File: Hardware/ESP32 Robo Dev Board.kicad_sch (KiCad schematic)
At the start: 49 parts, among them J2 Conn_01x02_Pin, Q1 DMP2045U, SW1 SW_Push_Dual_x2, SW2 SW_Push, U1 ESP32-S3-WROOM-1, U2 TCA9548ARGER, U8 MCP73831-2-OT, U9 AP2112K-3.3

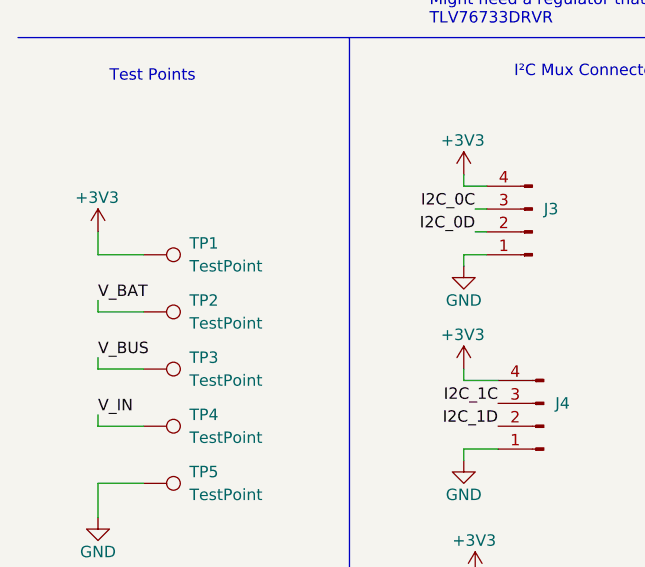
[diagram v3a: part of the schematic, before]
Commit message: Fix DRC Errors
Silkscreen overlapping and some trace width modification.
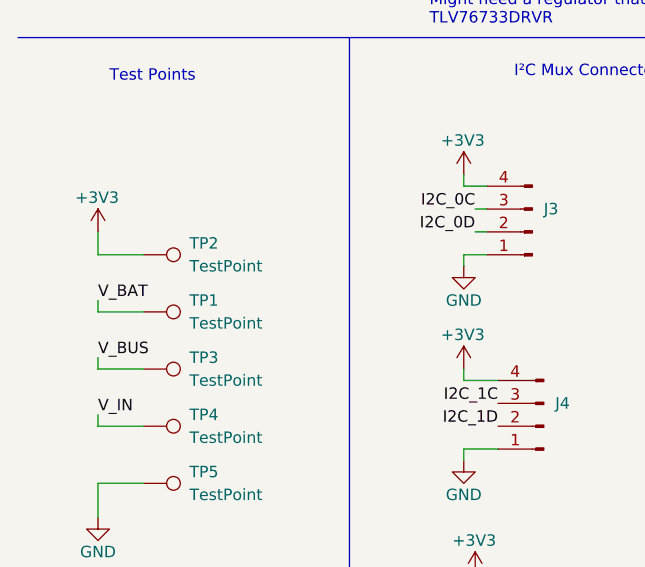
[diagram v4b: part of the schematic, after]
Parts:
- renumbered TP2 to TP1, TP1 to TP2
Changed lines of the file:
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@@
 		(dnp no)
 		(fields_autoplaced yes)
-		(property "Reference" "TP2"
-			(at 31.75 106.68 90)
+		(property "Reference" "TP1"
+			(at 31.75 106.6799 90)
 			(effects
 				(font
@@
 		)
 		(property "Value" "TestPoint"
-			(at 31.75 109.22 90)
+			(at 31.75 109.2199 90)
 			(effects
 				(font
@@
 			(project "ESP32 Robo Dev Board"
 				(path "/e63e39d7-6ac0-4ffd-8aa3-1841a4541b55"
-					(reference "TP2")
+					(reference "TP1")
 					(unit 1)
 				)
@@
 		(dnp no)
 		(fields_autoplaced yes)
-		(property "Reference" "TP1"
-			(at 31.75 100.33 90)
+		(property "Reference" "TP2"
+			(at 31.75 100.3299 90)
 			(effects
 				(font
@@
 		)
 		(property "Value" "TestPoint"
-			(at 31.75 102.87 90)
+			(at 31.75 102.8699 90)
 			(effects
 				(font
@@
 			(project "ESP32 Robo Dev Board"
 				(path "/e63e39d7-6ac0-4ffd-8aa3-1841a4541b55"
-					(reference "TP1")
-					(unit 1)
-				)
+					(reference "TP2")
+					(unit 1)
+				)

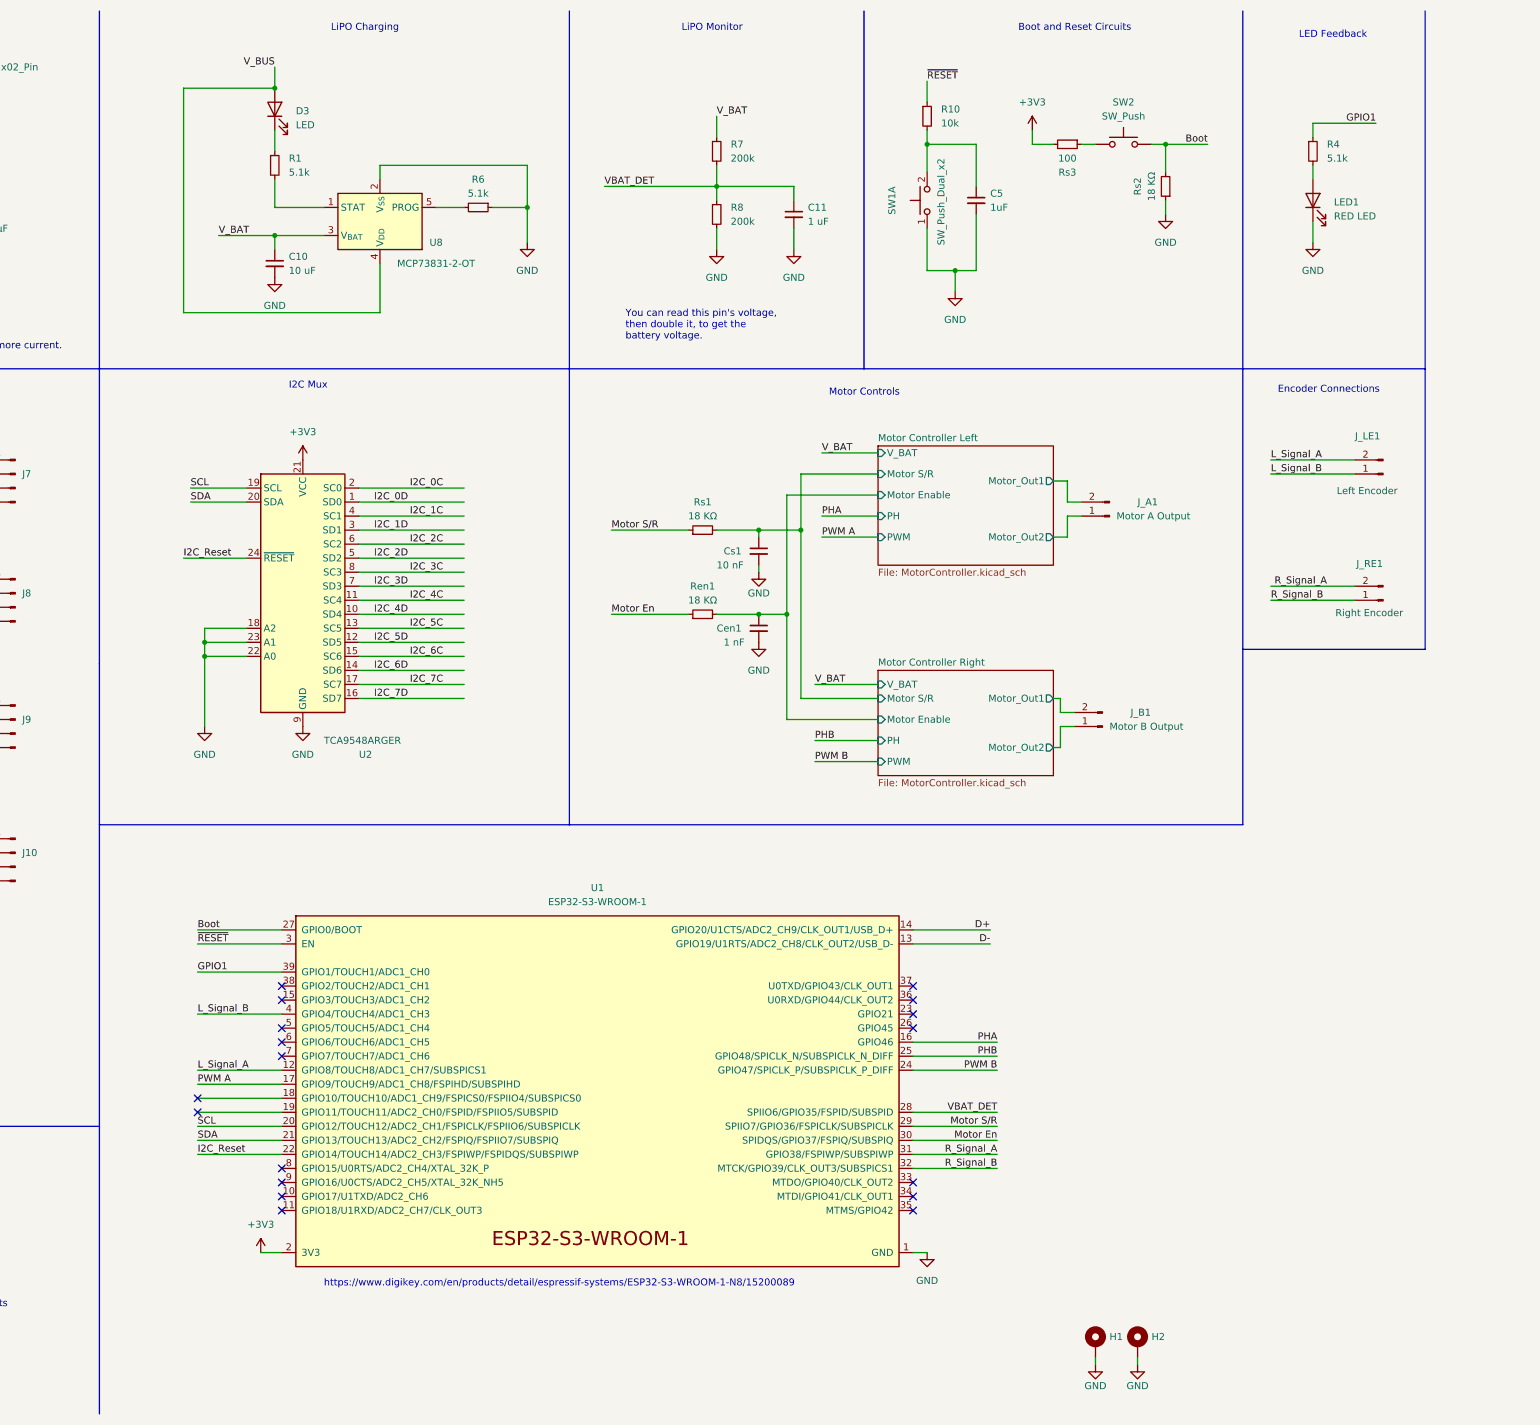
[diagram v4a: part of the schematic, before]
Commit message: Standardize I²C Bus and Route USB-C
Taking the opportunity to reroute and place STEMMA QT (JST-SH) Connectors to standardize the use of the I²C Multiplexer. Also took the chance to clean up the USB-C power supply and data line routing.
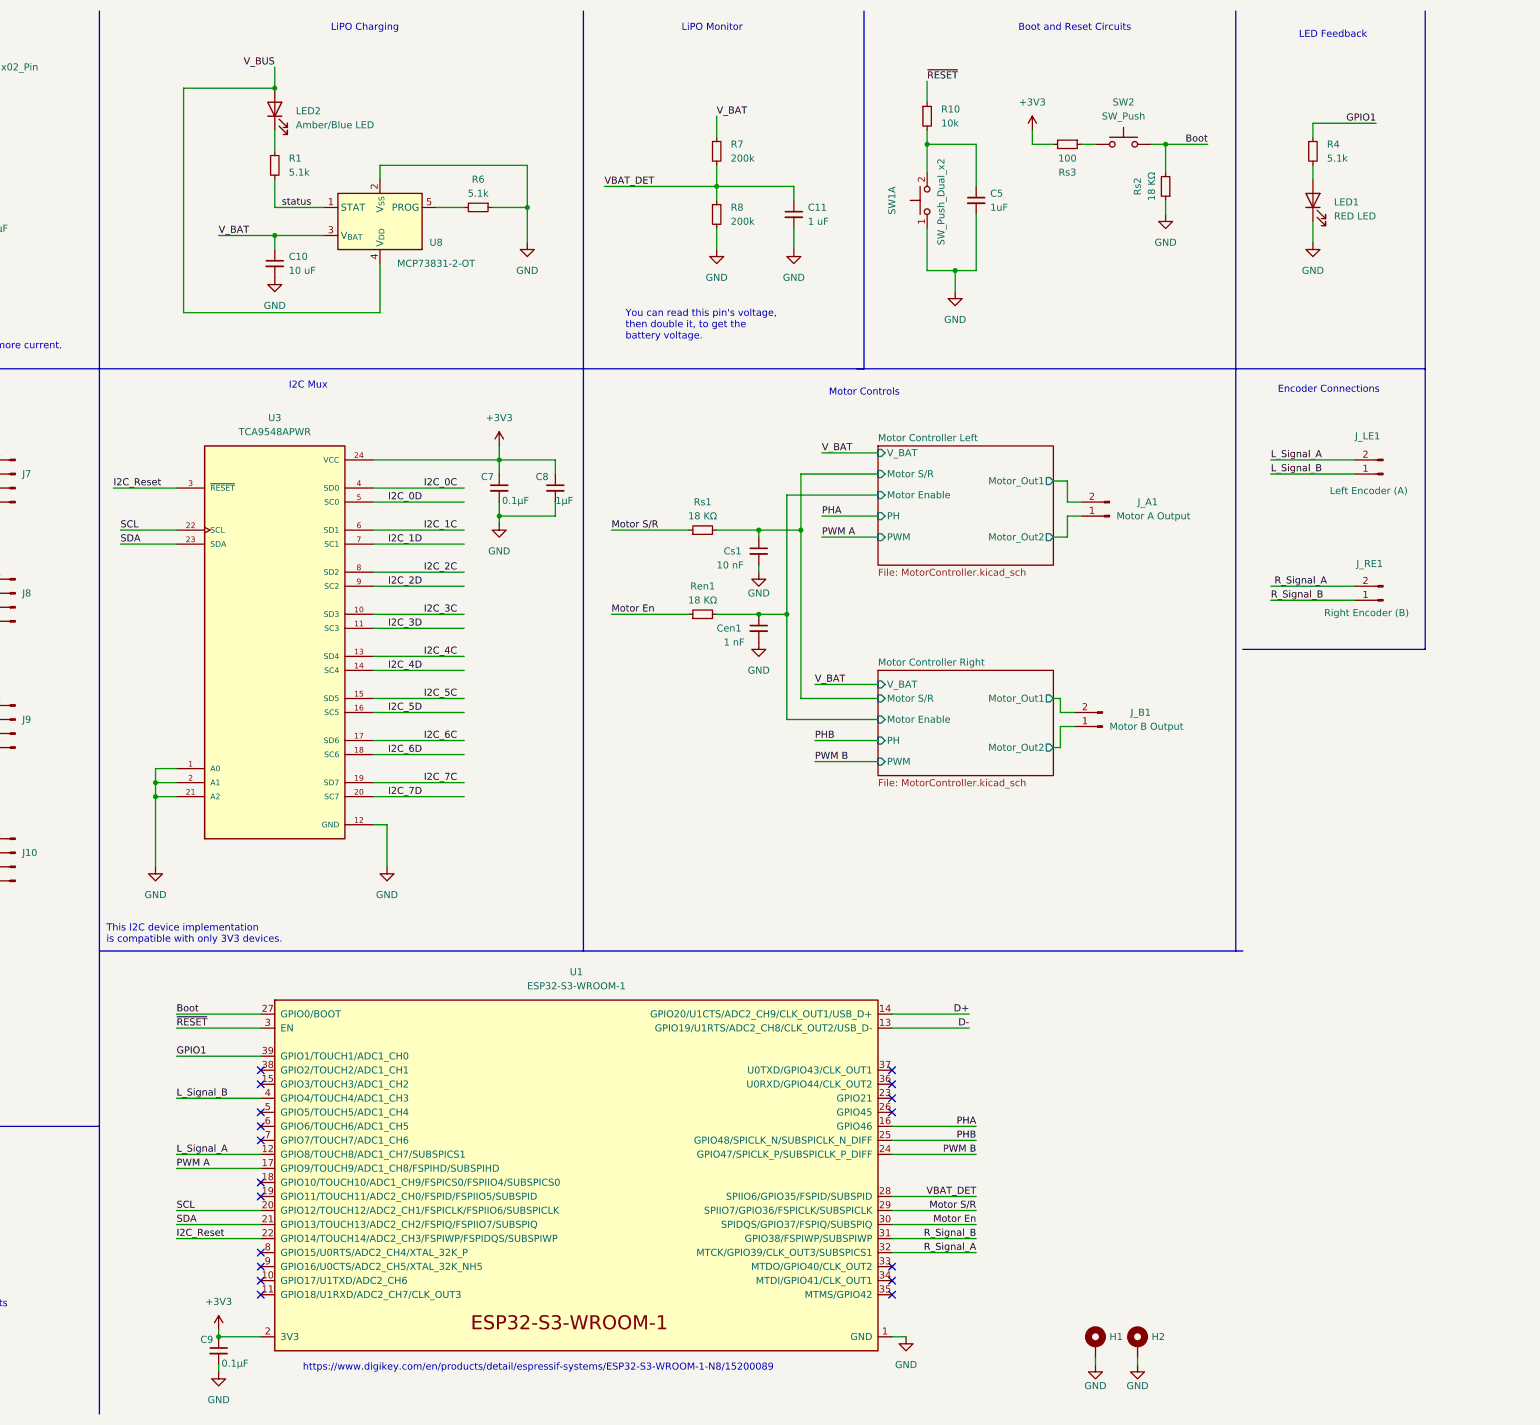
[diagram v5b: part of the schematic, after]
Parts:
- removed U2: TCA9548ARGER, Package_SO:TSSOP-24_4.4x7.8mm_P0.65mm, symbol Interface_Expansion:TCA9548ARGER
- added C7, C9: 0.1μF, Capacitor_SMD:C_0603_1608Metric, symbol Device:C_Small
- added C8: 1μF, Capacitor_SMD:C_0603_1608Metric, symbol Device:C_Small
- added U3: TCA9548APWR, TCA9548APWR:SOP65P640X120-24N, symbol TCA9548APWR:TCA9548APWR
- C1: footprint Capacitor_SMD:C_1206_3216Metric_Pad1.33x1.80mm_HandSolder -> Capacitor_SMD:C_0805_2012Metric
- J10, J3, J4, J5, J6, J7, J8, J9: footprint Connector_PinHeader_1.00mm:PinHeader_1x04_P1.00mm_Vertical -> Connector_JST:JST_SH_SM04B-SRSS-TB_1x04-1MP_P1.00mm_Horizontal
- J2: footprint Connector_PinHeader_1.27mm:PinHeader_1x02_P1.27mm_Vertical -> Connector_JST:JST_EH_B2B-EH-A_1x02_P2.50mm_Vertical
- J_LE1: value Left Encoder -> Left Encoder (A)
- J_RE1: value Right Encoder -> Right Encoder (B)
- LED2: renamed from D3; value LED -> Amber/Blue LED; footprint Resistor_SMD:R_0805_2012Metric -> LED_SMD:LED_0805_2012Metric
- R10, R2, R6: footprint Resistor_SMD:R_0805_2012Metric -> Resistor_SMD:R_0603_1608Metric
- R4: footprint Resistor_SMD:R_0805_2012Metric_Pad1.20x1.40mm_HandSolder -> Resistor_SMD:R_0603_1608Metric
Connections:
- net +3V3: now also C7.1, C8.1, C9.1, U3.24 (VCC)
- net GND: now also C7.2, C8.2, C9.2, U3.1 (A0), U3.12 (GND), U3.2 (A1), U3.21 (A2)
- net I2C_0C: now also U3.4 (SD0)
- net I2C_0D: now also U3.5 (SC0)
- net I2C_1C: now also U3.6 (SD1)
- net I2C_1D: now also U3.7 (SC1)
- net I2C_2C: now also U3.8 (SD2)
- net I2C_2D: now also U3.9 (SC2)
- net I2C_3C: now also U3.10 (SD3)
- net I2C_3D: now also U3.11 (SC3)
- net I2C_4C: now also U3.13 (SD4)
- net I2C_4D: now also U3.14 (SC4)
- net I2C_5C: now also U3.15 (SD5)
- net I2C_5D: now also U3.16 (SC5)
- net I2C_6C: now also U3.17 (SD6)
- net I2C_6D: now also U3.18 (SC6)
- net I2C_7C: now also U3.19 (SD7)
- net I2C_7D: now also U3.20 (SC7)
- net I2C_Reset: now also U3.3 (~{RESET})
- net R_Signal_A: now also U1.32 (MTCK/GPIO39/CLK_OUT3/SUBSPICS1); no longer U1.31 (GPIO38/FSPIWP/SUBSPIWP)
- net R_Signal_B: now also U1.31 (GPIO38/FSPIWP/SUBSPIWP); no longer U1.32 (MTCK/GPIO39/CLK_OUT3/SUBSPICS1)
- net SCL: now also U3.22 (SCL)
- net SDA: now also U3.23 (SDA)
- net status: now reaches R1.2, U8.1 (STAT)
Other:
- note added: "This I2C device implementation is compatible with only 3V3 devices."
- moved on the sheet: U1
